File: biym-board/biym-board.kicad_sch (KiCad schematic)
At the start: 1 part

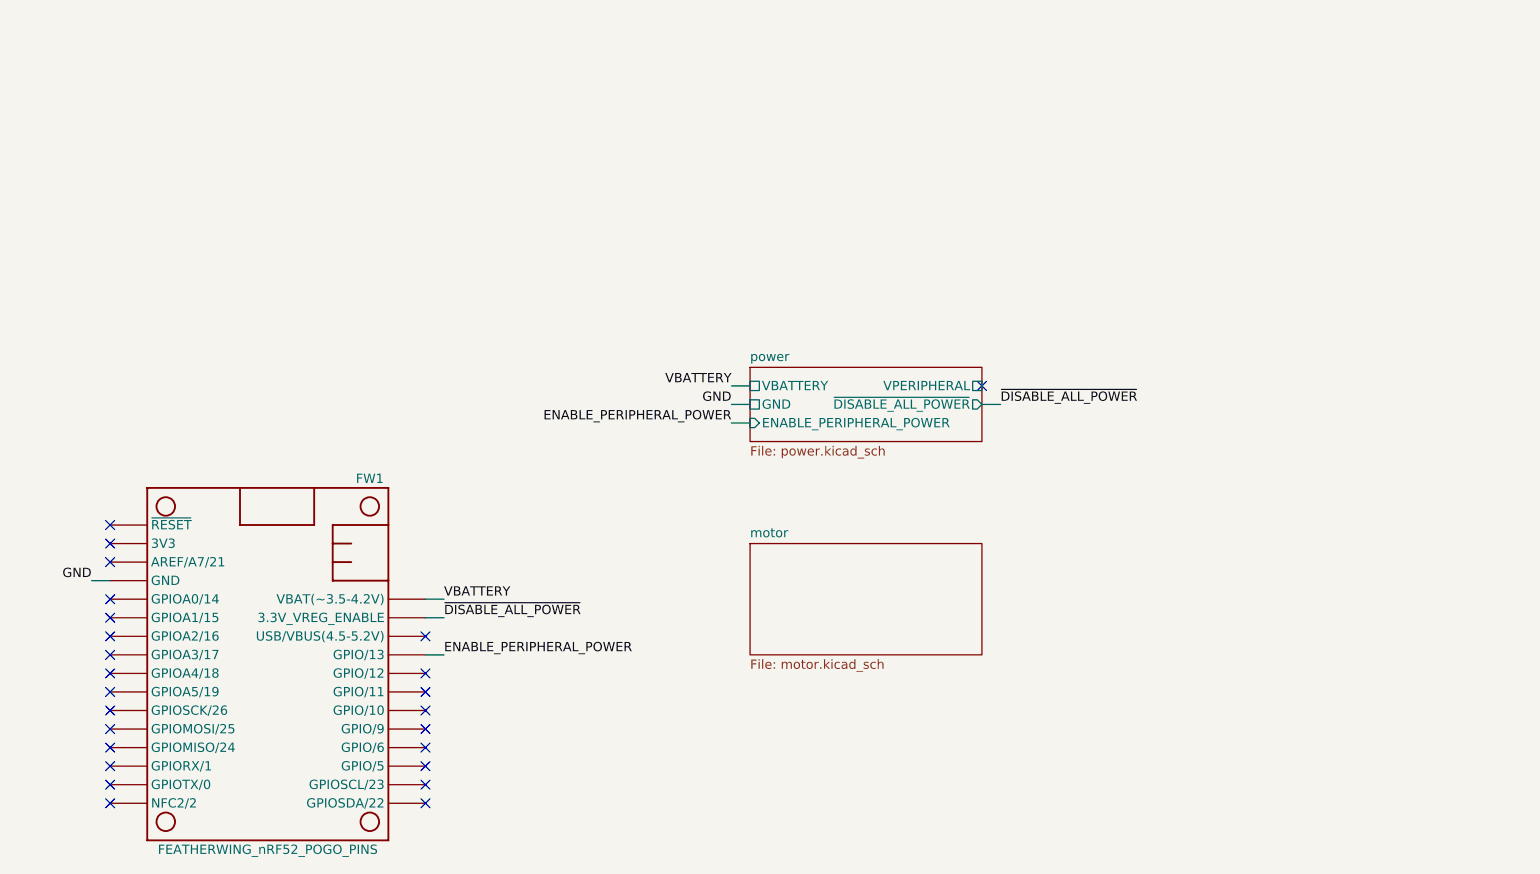
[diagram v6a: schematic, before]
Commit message: More motor driver wiring
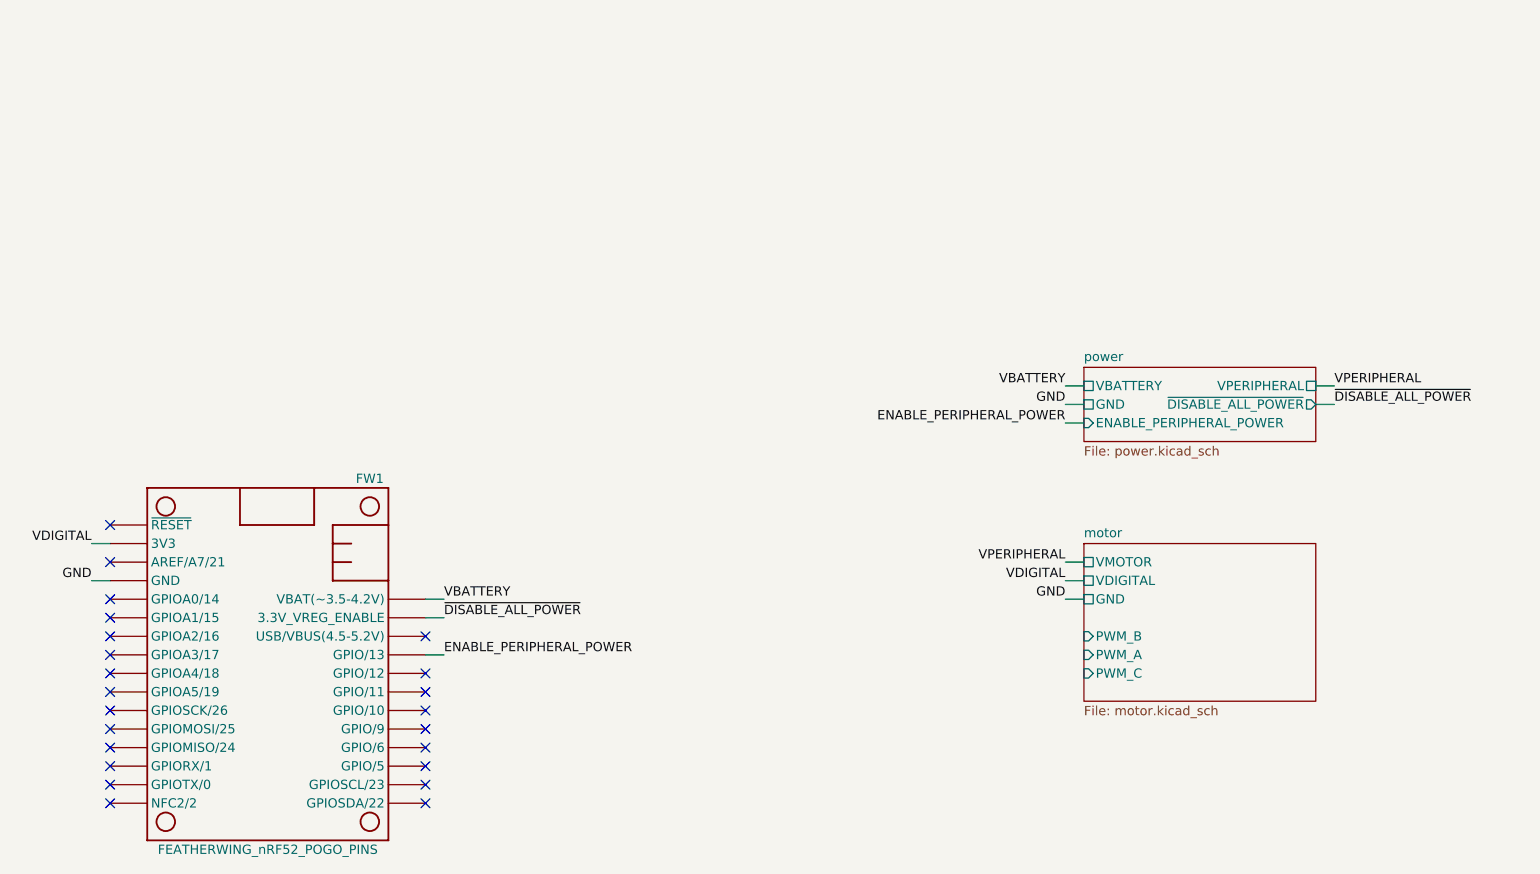
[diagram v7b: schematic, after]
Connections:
- net VDIGITAL: now reaches FW1.2 (3V3)
- no-connect marks 25 -> 23
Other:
- sheet motor ports: added GND, PWM_A, PWM_B, PWM_C, VDIGITAL, VMOTOR; removed none
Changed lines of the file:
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@@
   (no_connect (at 49.53 115.57))
   (no_connect (at 49.53 97.79))
-  (no_connect (at 168.91 68.58))
   (no_connect (at 49.53 107.95))
   (no_connect (at 49.53 100.33))
-  (no_connect (at 49.53 90.17))
   (wire (pts (xy 92.71 97.79) (xy 95.25 97.79))
     (stroke (width 0) (type default) (color 0 0 0 0))
@@
     (stroke (width 0) (type default) (color 0 0 0 0))
   )
-  (wire (pts (xy 134.62 71.12) (xy 137.16 71.12))
-    (stroke (width 0) (type default) (color 0 0 0 0))
-  )
-  (wire (pts (xy 168.91 71.12) (xy 171.45 71.12))
+  (wire (pts (xy 180.34 71.12) (xy 182.88 71.12))
+    (stroke (width 0) (type default) (color 0 0 0 0))
+  )
+  (wire (pts (xy 180.34 97.79) (xy 182.88 97.79))
+    (stroke (width 0) (type default) (color 0 0 0 0))
+  )
+  (wire (pts (xy 182.88 92.71) (xy 180.34 92.71))
+    (stroke (width 0) (type default) (color 0 0 0 0))
+  )
+  (wire (pts (xy 214.63 71.12) (xy 217.17 71.12))
     (stroke (width 0) (type default) (color 0 0 0 0))
   )
@@
     (stroke (width 0) (type default) (color 0 0 0 0))
   )
-  (wire (pts (xy 137.16 73.66) (xy 134.62 73.66))
-    (stroke (width 0) (type default) (color 0 0 0 0))
-  )
-  (wire (pts (xy 137.16 68.58) (xy 134.62 68.58))
+  (wire (pts (xy 182.88 73.66) (xy 180.34 73.66))
+    (stroke (width 0) (type default) (color 0 0 0 0))
+  )
+  (wire (pts (xy 180.34 95.25) (xy 182.88 95.25))
+    (stroke (width 0) (type default) (color 0 0 0 0))
+  )
+  (wire (pts (xy 214.63 68.58) (xy 217.17 68.58))
+    (stroke (width 0) (type default) (color 0 0 0 0))
+  )
+  (wire (pts (xy 182.88 68.58) (xy 180.34 68.58))
+    (stroke (width 0) (type default) (color 0 0 0 0))
+  )
+  (wire (pts (xy 46.99 90.17) (xy 49.53 90.17))
     (stroke (width 0) (type default) (color 0 0 0 0))
   )
@@
     (effects (font (size 1.27 1.27)) (justify left bottom))
   )
-  (label "GND" (at 134.62 71.12 180)
-    (effects (font (size 1.27 1.27)) (justify right bottom))
-  )
-  (label "ENABLE_PERIPHERAL_POWER" (at 134.62 73.66 180)
+  (label "VPERIPHERAL" (at 217.17 68.58 0)
+    (effects (font (size 1.27 1.27)) (justify left bottom))
+  )
+  (label "GND" (at 180.34 71.12 180)
+    (effects (font (size 1.27 1.27)) (justify right bottom))
+  )
+  (label "ENABLE_PERIPHERAL_POWER" (at 180.34 73.66 180)
     (effects (font (size 1.27 1.27)) (justify right bottom))
   )
@@
     (effects (font (size 1.27 1.27)) (justify right bottom))
   )
-  (label "VBATTERY" (at 134.62 68.58 180)
-    (effects (font (size 1.27 1.27)) (justify right bottom))
-  )
-  (label "~{DISABLE_ALL_POWER}" (at 171.45 71.12 0)
-    (effects (font (size 1.27 1.27)) (justify left bottom))
+  (label "VBATTERY" (at 180.34 68.58 180)
+    (effects (font (size 1.27 1.27)) (justify right bottom))
+  )
+  (label "VPERIPHERAL" (at 180.34 92.71 180)
+    (effects (font (size 1.27 1.27)) (justify right bottom))
+  )
+  (label "~{DISABLE_ALL_POWER}" (at 217.17 71.12 0)
+    (effects (font (size 1.27 1.27)) (justify left bottom))
+  )
+  (label "VDIGITAL" (at 180.34 95.25 180)
+    (effects (font (size 1.27 1.27)) (justify right bottom))
   )
   (label "~{DISABLE_ALL_POWER}" (at 95.25 100.33 0)
     (effects (font (size 1.27 1.27)) (justify left bottom))
+  )
+  (label "GND" (at 180.34 97.79 180)
+    (effects (font (size 1.27 1.27)) (justify right bottom))
+  )
+  (label "VDIGITAL" (at 46.99 90.17 180)
+    (effects (font (size 1.27 1.27)) (justify right bottom))
   )
   (label "VBATTERY" (at 95.25 97.79 0)
@@
     (pin "9")
   )
-  (sheet (at 137.16 66.04) (size 31.75 10.16) (fields_autoplaced)
+  (sheet (at 182.88 66.04) (size 31.75 10.16) (fields_autoplaced)
     (stroke (width 0.1524) (type solid) (color 0 0 0 0))
     (fill (color 0 0 0 0.0000))
-    (property "Sheet name" "power" (id 0) (at 137.16 65.3284 0)
+    (property "Sheet name" "power" (id 0) (at 182.88 65.3284 0)
       (effects (font (size 1.27 1.27)) (justify left bottom))
     )
-    (property "Sheet file" "power.kicad_sch" (id 1) (at 137.16 76.7846 0)
+    (property "Sheet file" "power.kicad_sch" (id 1) (at 182.88 76.7846 0)
       (effects (font (size 1.27 1.27)) (justify left top))
     )
-    (pin "GND" passive (at 137.16 71.12 180)
-      (effects (font (size 1.27 1.27)) (justify left))
-    )
-    (pin "VPERIPHERAL" passive (at 168.91 68.58 0)
+    (pin "GND" passive (at 182.88 71.12 180)
+      (effects (font (size 1.27 1.27)) (justify left))
+    )
+    (pin "VPERIPHERAL" passive (at 214.63 68.58 0)
       (effects (font (size 1.27 1.27)) (justify right))
     )
-    (pin "VBATTERY" passive (at 137.16 68.58 180)
-      (effects (font (size 1.27 1.27)) (justify left))
-    )
-    (pin "~{DISABLE_ALL_POWER}" output (at 168.91 71.12 0)
+    (pin "VBATTERY" passive (at 182.88 68.58 180)
+      (effects (font (size 1.27 1.27)) (justify left))
+    )
+    (pin "~{DISABLE_ALL_POWER}" output (at 214.63 71.12 0)
       (effects (font (size 1.27 1.27)) (justify right))
     )
-    (pin "ENABLE_PERIPHERAL_POWER" input (at 137.16 73.66 180)
-      (effects (font (size 1.27 1.27)) (justify left))
-    )
-  )
-  (sheet (at 137.16 90.17) (size 31.75 15.24) (fields_autoplaced)
+    (pin "ENABLE_PERIPHERAL_POWER" input (at 182.88 73.66 180)
+      (effects (font (size 1.27 1.27)) (justify left))
+    )
+  )
+  (sheet (at 182.88 90.17) (size 31.75 21.59) (fields_autoplaced)
     (stroke (width 0.1524) (type solid) (color 0 0 0 0))
     (fill (color 0 0 0 0.0000))
-    (property "Sheet name" "motor" (id 0) (at 137.16 89.4584 0)
+    (property "Sheet name" "motor" (id 0) (at 182.88 89.4584 0)
       (effects (font (size 1.27 1.27)) (justify left bottom))
     )
-    (property "Sheet file" "motor.kicad_sch" (id 1) (at 137.16 105.9946 0)
+    (property "Sheet file" "motor.kicad_sch" (id 1) (at 182.88 112.3446 0)
       (effects (font (size 1.27 1.27)) (justify left top))
+    )
+    (pin "VDIGITAL" passive (at 182.88 95.25 180)
+      (effects (font (size 1.27 1.27)) (justify left))
+    )
+    (pin "VMOTOR" passive (at 182.88 92.71 180)
+      (effects (font (size 1.27 1.27)) (justify left))
+    )
+    (pin "GND" passive (at 182.88 97.79 180)
+      (effects (font (size 1.27 1.27)) (justify left))
+    )
+    (pin "PWM_B" input (at 182.88 102.87 180)
+      (effects (font (size 1.27 1.27)) (justify left))
+    )
+    (pin "PWM_A" input (at 182.88 105.41 180)
+      (effects (font (size 1.27 1.27)) (justify left))
+    )
+    (pin "PWM_C" input (at 182.88 107.95 180)
+      (effects (font (size 1.27 1.27)) (justify left))
     )
   )
@@
       (reference "R1") (unit 1) (value "100k") (footprint "Janelia:SM0402")
     )
-  )
+    (path "/79116d11-26fd-48fc-b8f9-7a7b774125a1/da95f1b2-1af2-47f6-bf0e-981916e2aac9"
+      (reference "U?") (unit 1) (value "DRV8311H") (footprint "Janelia:WQFN-24-1EP_3x3mm_P0.4mm_EP1.9x1.9mm_ThermalVias")
+    )
+  )

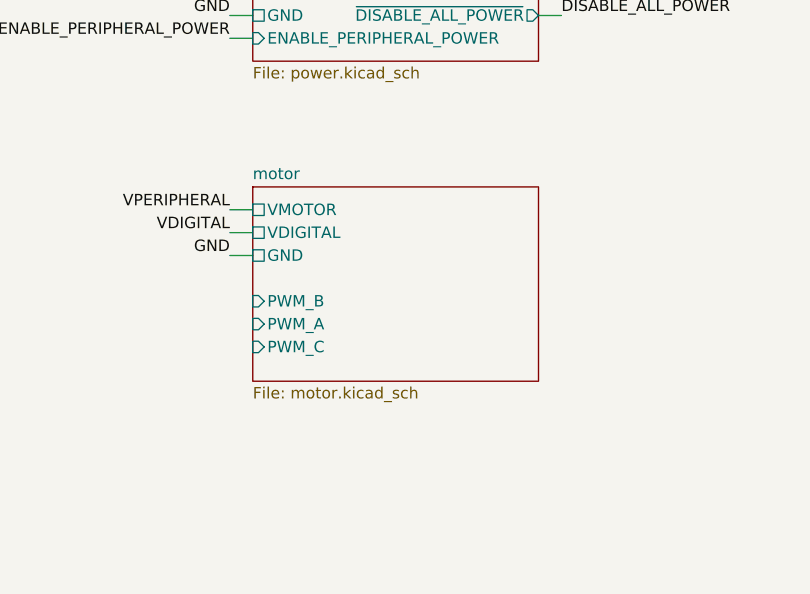
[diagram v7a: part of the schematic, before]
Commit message: Rename reference files
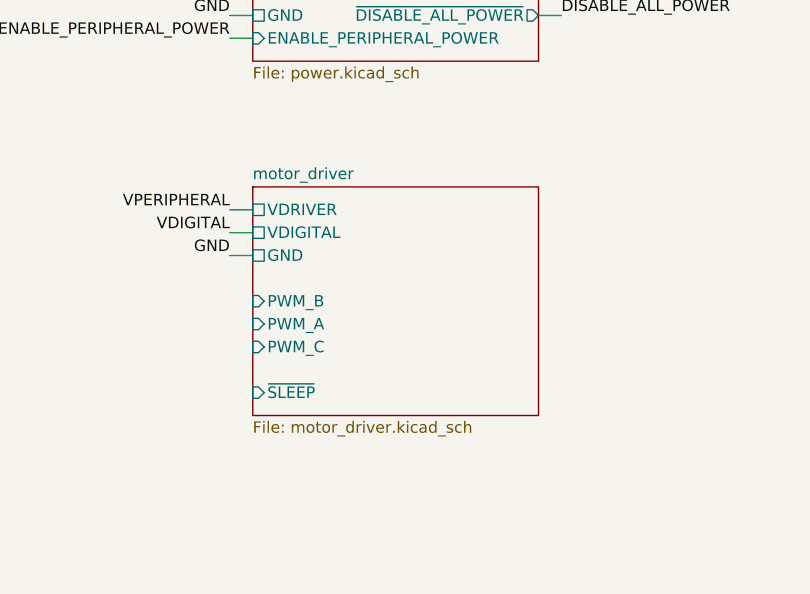
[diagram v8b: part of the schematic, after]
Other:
- sheet motor renamed motor_driver
- sheet motor_driver: file motor.kicad_sch -> motor_driver.kicad_sch
- sheet motor_driver ports: added VDRIVER, ~{SLEEP}; removed VMOTOR
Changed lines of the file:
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@@
     )
   )
-  (sheet (at 182.88 90.17) (size 31.75 21.59) (fields_autoplaced)
+  (sheet (at 182.88 90.17) (size 31.75 25.4) (fields_autoplaced)
     (stroke (width 0.1524) (type solid) (color 0 0 0 0))
     (fill (color 0 0 0 0.0000))
-    (property "Sheet name" "motor" (id 0) (at 182.88 89.4584 0)
+    (property "Sheet name" "motor_driver" (id 0) (at 182.88 89.4584 0)
       (effects (font (size 1.27 1.27)) (justify left bottom))
     )
-    (property "Sheet file" "motor.kicad_sch" (id 1) (at 182.88 112.3446 0)
+    (property "Sheet file" "motor_driver.kicad_sch" (id 1) (at 182.88 116.1546 0)
       (effects (font (size 1.27 1.27)) (justify left top))
     )
     (pin "VDIGITAL" passive (at 182.88 95.25 180)
-      (effects (font (size 1.27 1.27)) (justify left))
-    )
-    (pin "VMOTOR" passive (at 182.88 92.71 180)
       (effects (font (size 1.27 1.27)) (justify left))
     )
@@
       (effects (font (size 1.27 1.27)) (justify left))
     )
+    (pin "~{SLEEP}" input (at 182.88 113.03 180)
+      (effects (font (size 1.27 1.27)) (justify left))
+    )
+    (pin "VDRIVER" passive (at 182.88 92.71 180)
+      (effects (font (size 1.27 1.27)) (justify left))
+    )
   )
   (sheet_instances
@@
       (reference "FW1") (unit 1) (value "FEATHERWING_nRF52_POGO_PINS") (footprint "Janelia:FEATHERWING_POGO_PINS")
     )
-    (path "/2c398cb1-cb17-49ba-86d6-22731656ead9/ee181020-0a66-4e94-8afa-04e718523ff4"
-      (reference "J1") (unit 1) (value "JST_SH_BM02_VERTICAL") (footprint "Janelia:JST_SH_BM02B-SRSS-TB_1x02-1MP_P1.00mm_Vertical")
+    (path "/2c398cb1-cb17-49ba-86d6-22731656ead9/be169668-1ccd-45d2-bc9d-fec61d1f06d0"
+      (reference "J1") (unit 1) (value "HEADER_01X02_JST_SH_SMD_VERTICAL") (footprint "Janelia:JST_SH_BM02B-SRSS-TB_1x02-1MP_P1.00mm_Vertical")
+    )
+    (path "/79116d11-26fd-48fc-b8f9-7a7b774125a1/73049e1e-00b1-4d86-b27f-13c3a3887bed"
+      (reference "J?") (unit 1) (value "HEADER_01X03_JST_PH_VERTICAL") (footprint "Janelia:JST_PH_B3B-PH-K_1x03_P2.00mm_Vertical")
     )
     (path "/2c398cb1-cb17-49ba-86d6-22731656ead9/ab142e9c-269c-4749-bf0a-3cc0397cc4cb"
